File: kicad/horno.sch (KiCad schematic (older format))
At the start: 3 parts, among them P4 CONN_01X02, Q1 BC547

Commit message: modificaciones del proyecto Kicad
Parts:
- added P7: CONN_02X11, Pin_Headers:Pin_Header_Straight_2x11, symbol CONN_02X11
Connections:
- new net LCD_D0: P7.7 (P7)
- new net LCD_D1: P7.8 (P8)
- new net LCD_D2: P7.9 (P9)
- new net LCD_D3: P7.10 (P10)
- new net LCD_D4: P7.11 (P11)
- new net LCD_D5: P7.12 (P12)
- new net LCD_D6: P7.13 (P13)
- new net LCD_D7: P7.14 (P14)
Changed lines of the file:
@@
 encoding utf-8
 Sheet 1 5
-Title "Circuitos digital y analógicos"
+Title "Esquemático jerárquico"
 Date "2016-08-27"
 Rev "1"
@@
 S 2100 3700 1400 850
 U 57C2159A
-F0 "Amplificador LM35" 60
+F0 "LM35" 60
 F1 "AmpLM35.sch" 60
 F2 "+5V" I L 2100 3800 60
@@
 F5 "LM35_OUT" O R 3500 3950 60
 $EndSheet
-Wire Wire Line
-	3500 3950 4300 3950
 $Sheet
 S 2100 2700 1400 750
 U 57C52EB8
-F0 "Amplificador Termocupla" 60
+F0 "Termocupla" 60
 F1 "AmpTermocupla.sch" 60
 F2 "TERMOCUPLA_OUT" O R 3500 2800 60
@@
 F5 "GND" I L 2100 3350 60
 $EndSheet
-Wire Wire Line
-	3500 2800 3850 2800
-Wire Wire Line
-	3850 2800 3850 3850
-Wire Wire Line
-	3850 3850 4300 3850
 $Sheet
 S 6300 4550 1100 1450
 U 57C5E497
-F0 "Driver del motor paso a paso" 60
+F0 "Motor paso a paso" 60
 F1 "motorPP.sch" 60
 F2 "S1" I L 6300 5050 60
@@
 	0    1    1    0
 $EndComp
-Wire Wire Line
-	5450 3300 5850 3300
 $Comp
 L BC547 Q1
@@
 F 0 "Q1" H 6800 3375 50  0000 L CNN
 F 1 "BC547" H 6800 3300 50  0000 L CNN
-F 2 "TO_SOT_Packages_THT:TO-92_Inline_Narrow_Oval" H 6800 3225 50  0000 L CIN
+F 2 "TO_SOT_Packages_THT:TO-92_Inline_Narrow_Oval" H 6800 3225 50  0001 L CIN
 F 3 "" H 6600 3300 50  0000 L CNN
 	1    6600 3300
 	1    0    0    -1
 $EndComp
-Wire Wire Line
-	6150 3300 6400 3300
 $Comp
 L GND #PWR01
@@
 	1    0    0    -1
 $EndComp
-Wire Wire Line
-	6700 3500 6700 3650
 $Comp
 L CONN_01X02 P4
@@
 	1    0    0    -1
 $EndComp
+$Comp
+L CONN_02X11 P7
+U 1 1 57C3EF67
+P 2350 6650
+F 0 "P7" H 2350 7250 50  0000 C CNN
+F 1 "CONN_02X11" V 2350 6650 50  0000 C CNN
+F 2 "Pin_Headers:Pin_Header_Straight_2x11" H 2350 5450 50  0001 C CNN
+F 3 "" H 2350 5450 50  0000 C CNN
+	1    2350 6650
+	1    0    0    -1
+$EndComp
+Wire Wire Line
+	3500 3950 4300 3950
+Wire Wire Line
+	3500 2800 3850 2800
+Wire Wire Line
+	3850 2800 3850 3850
+Wire Wire Line
+	3850 3850 4300 3850
+Wire Wire Line
+	5450 3300 5850 3300
+Wire Wire Line
+	6150 3300 6400 3300
+Wire Wire Line
+	6700 3500 6700 3650
 Wire Wire Line
 	6700 2300 6700 2600
@@
 Wire Wire Line
 	5450 5350 6300 5350
+Wire Wire Line
+	4300 4700 3650 4700
+Wire Wire Line
+	4300 4800 3650 4800
+Wire Wire Line
+	4300 4900 3650 4900
+Wire Wire Line
+	4300 5000 3650 5000
+Wire Wire Line
+	4300 5100 3650 5100
+Text Label 3650 4700 0    60   ~ 0
+LCD_D0
+Text Label 3650 4800 0    60   ~ 0
+LCD_D1
+Text Label 3650 4900 0    60   ~ 0
+LCD_D2
+Text Label 3650 5000 0    60   ~ 0
+LCD_D3
+Text Label 3650 5100 0    60   ~ 0
+LCD_D4
+Wire Wire Line
+	4300 5200 3650 5200
+Wire Wire Line
+	4300 5300 3650 5300
+Wire Wire Line
+	4300 5400 3650 5400
+Text Label 3650 5200 0    60   ~ 0
+LCD_D5
+Text Label 3650 5300 0    60   ~ 0
+LCD_D6
+Text Label 3650 5400 0    60   ~ 0
+LCD_D7
+Wire Wire Line
+	2100 6450 1650 6450
+Text Label 1650 6450 0    60   ~ 0
+LCD_D0
+Wire Wire Line
+	2100 6550 1650 6550
+Wire Wire Line
+	2100 6650 1650 6650
+Wire Wire Line
+	2100 6750 1650 6750
+Wire Wire Line
+	2600 6450 3050 6450
+Text Label 3050 6450 2    60   ~ 0
+LCD_D1
+Wire Wire Line
+	2600 6550 3050 6550
+Wire Wire Line
+	2600 6650 3050 6650
+Wire Wire Line
+	2600 6750 3050 6750
+Text Label 3050 6550 2    60   ~ 0
+LCD_D3
+Text Label 3050 6650 2    60   ~ 0
+LCD_D5
+Text Label 3050 6750 2    60   ~ 0
+LCD_D7
+Text Label 1650 6550 0    60   ~ 0
+LCD_D2
+Text Label 1650 6650 0    60   ~ 0
+LCD_D4
+Text Label 1650 6750 0    60   ~ 0
+LCD_D6
 $EndSCHEMATC

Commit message: circuito y pcb terminado.
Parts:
- added P10: Alimentación, Pin_Headers:Pin_Header_Straight_1x03, symbol CONN_01X03
- P4: value CONN_01X02 -> TRIAC
- P7: value CONN_02X11 -> Pantalla
- Q1: footprint TO_SOT_Packages_THT:TO-92_Inline_Narrow_Oval -> TO_SOT_Packages_THT:TO-92_Inline_Wide
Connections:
- net +5V: now also P7.2 (P2), P10.2 (P2)
- net GND: now also P7.1 (P1), P10.1 (P1)
- net LCD_CS: now reaches P7.15 (P15)
- net LCD_RST: now reaches P7.16 (P16)
- net LCD_RD: now reaches P7.4 (P4)
- net LCD_WR: now reaches P7.5 (P5)
- net LCD_A0: now reaches P7.6 (P6)
- new net -5V: P10.3 (P3)
- no-connect marks 0 -> 7
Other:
- note added: "Conector de la\nllave semiconductora"
- note added: "Conector de la\npantalla LCD"
- note added: "Entrada de \nalimentación"
- moved on the sheet: P4, Q1, R9

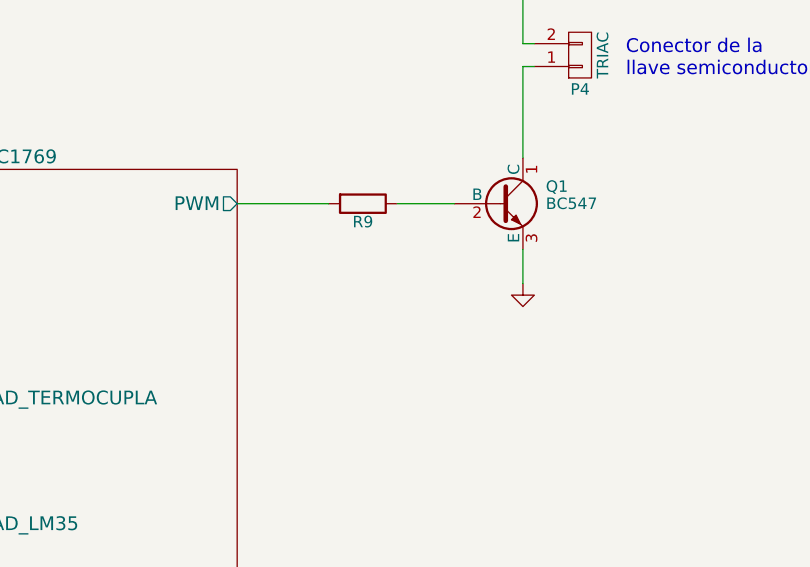
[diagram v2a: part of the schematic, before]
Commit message: R de pulldown para que la resistencia no se energice con un reset.
Cuando el microcontrolador está pasando por un reset, la pata del PWM está flotando y alcanza para activar el transistor.
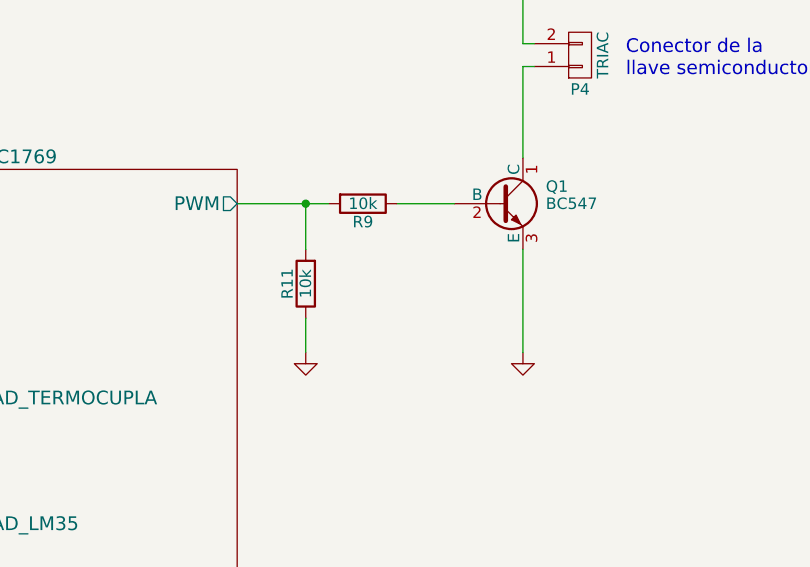
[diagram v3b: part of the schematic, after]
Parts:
- added R11: 10k, Resistors_ThroughHole:Resistor_Horizontal_RM10mm, symbol R
- R9: value R -> 10k
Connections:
- net GND: now also R11.1
- net LPC1769/PWM: now also R11.2
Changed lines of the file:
@@
 P 6000 2550
 F 0 "R9" V 6080 2550 50  0000 C CNN
-F 1 "R" V 6000 2550 50  0001 C CNN
+F 1 "10k" V 6000 2550 50  0000 C CNN
 F 2 "Resistors_ThroughHole:Resistor_Horizontal_RM10mm" V 5930 2550 50  0001 C CNN
 F 3 "" H 6000 2550 50  0000 C CNN
@@
 $EndComp
 $Comp
-L GND #PWR01
+L GND #PWR5
 U 1 1 57C67CA4
-P 6700 2900
-F 0 "#PWR01" H 6700 2650 50  0001 C CNN
-F 1 "GND" H 6700 2750 50  0001 C CNN
-F 2 "" H 6700 2900 50  0000 C CNN
-F 3 "" H 6700 2900 50  0000 C CNN
-	1    6700 2900
+P 6700 3200
+F 0 "#PWR5" H 6700 2950 50  0001 C CNN
+F 1 "GND" H 6700 3050 50  0001 C CNN
+F 2 "" H 6700 3200 50  0000 C CNN
+F 3 "" H 6700 3200 50  0000 C CNN
+	1    6700 3200
 	1    0    0    -1
 $EndComp
@@
 $EndComp
 $Comp
-L +5V #PWR02
+L +5V #PWR4
 U 1 1 57C682C4
 P 6700 1550
-F 0 "#PWR02" H 6700 1400 50  0001 C CNN
+F 0 "#PWR4" H 6700 1400 50  0001 C CNN
 F 1 "+5V" H 6700 1690 50  0000 C CNN
 F 2 "" H 6700 1550 50  0000 C CNN
@@
 	6150 2550 6400 2550
 Wire Wire Line
-	6700 2750 6700 2900
+	6700 2750 6700 3200
 Wire Wire Line
 	6700 1550 6700 1850
@@
 LCD_D6
 $Comp
-L GND #PWR03
+L GND #PWR1
 U 1 1 57C97FEB
 P 1400 6150
-F 0 "#PWR03" H 1400 5900 50  0001 C CNN
+F 0 "#PWR1" H 1400 5900 50  0001 C CNN
 F 1 "GND" H 1400 6000 50  0000 C CNN
 F 2 "" H 1400 6150 50  0000 C CNN
@@
 	2600 6150 3200 6150
 $Comp
-L +5V #PWR04
+L +5V #PWR2
 U 1 1 57C987B0
 P 3200 5950
-F 0 "#PWR04" H 3200 5800 50  0001 C CNN
+F 0 "#PWR2" H 3200 5800 50  0001 C CNN
 F 1 "+5V" H 3200 6090 50  0000 C CNN
 F 2 "" H 3200 5950 50  0000 C CNN
@@
 $EndComp
 $Comp
-L GND #PWR05
+L GND #PWR8
 U 1 1 57CBC9F7
 P 9850 2850
-F 0 "#PWR05" H 9850 2600 50  0001 C CNN
+F 0 "#PWR8" H 9850 2600 50  0001 C CNN
 F 1 "GND" H 9850 2700 50  0000 C CNN
 F 2 "" H 9850 2850 50  0000 C CNN
@@
 	9850 2650 9850 2850
 $Comp
-L +5V #PWR06
+L +5V #PWR6
 U 1 1 57CBD60F
 P 9650 2300
-F 0 "#PWR06" H 9650 2150 50  0001 C CNN
+F 0 "#PWR6" H 9650 2150 50  0001 C CNN
 F 1 "+5V" H 9650 2440 50  0000 C CNN
 F 2 "" H 9650 2300 50  0000 C CNN
@@
 $EndComp
 $Comp
-L -5V #PWR6
+L -5V #PWR7
 U 1 1 57CBD782
 P 9850 2300
-F 0 "#PWR6" H 9850 2400 50  0001 C CNN
+F 0 "#PWR7" H 9850 2400 50  0001 C CNN
 F 1 "-5V" H 9850 2450 50  0000 C CNN
 F 2 "" H 9850 2300 50  0000 C CNN
@@
 Wire Wire Line
 	9650 2550 9650 2300
+$Comp
+L R R11
+U 1 1 581CDAE7
+P 5750 2900
+F 0 "R11" V 5830 2900 50  0000 C CNN
+F 1 "10k" V 5750 2900 50  0000 C CNN
+F 2 "Resistors_ThroughHole:Resistor_Horizontal_RM10mm" V 5680 2900 50  0001 C CNN
+F 3 "" H 5750 2900 50  0000 C CNN
+	1    5750 2900
+	-1   0    0    1
+$EndComp
+Wire Wire Line
+	5750 2750 5750 2550
+Connection ~ 5750 2550
+Wire Wire Line
+	5750 3200 5750 3050
+$Comp
+L GND #PWR?
+U 1 1 581CDFB6
+P 5750 3200
+F 0 "#PWR?" H 5750 2950 50  0001 C CNN
+F 1 "GND" H 5750 3050 50  0001 C CNN
+F 2 "" H 5750 3200 50  0000 C CNN
+F 3 "" H 5750 3200 50  0000 C CNN
+	1    5750 3200
+	1    0    0    -1
+$EndComp
 $EndSCHEMATC

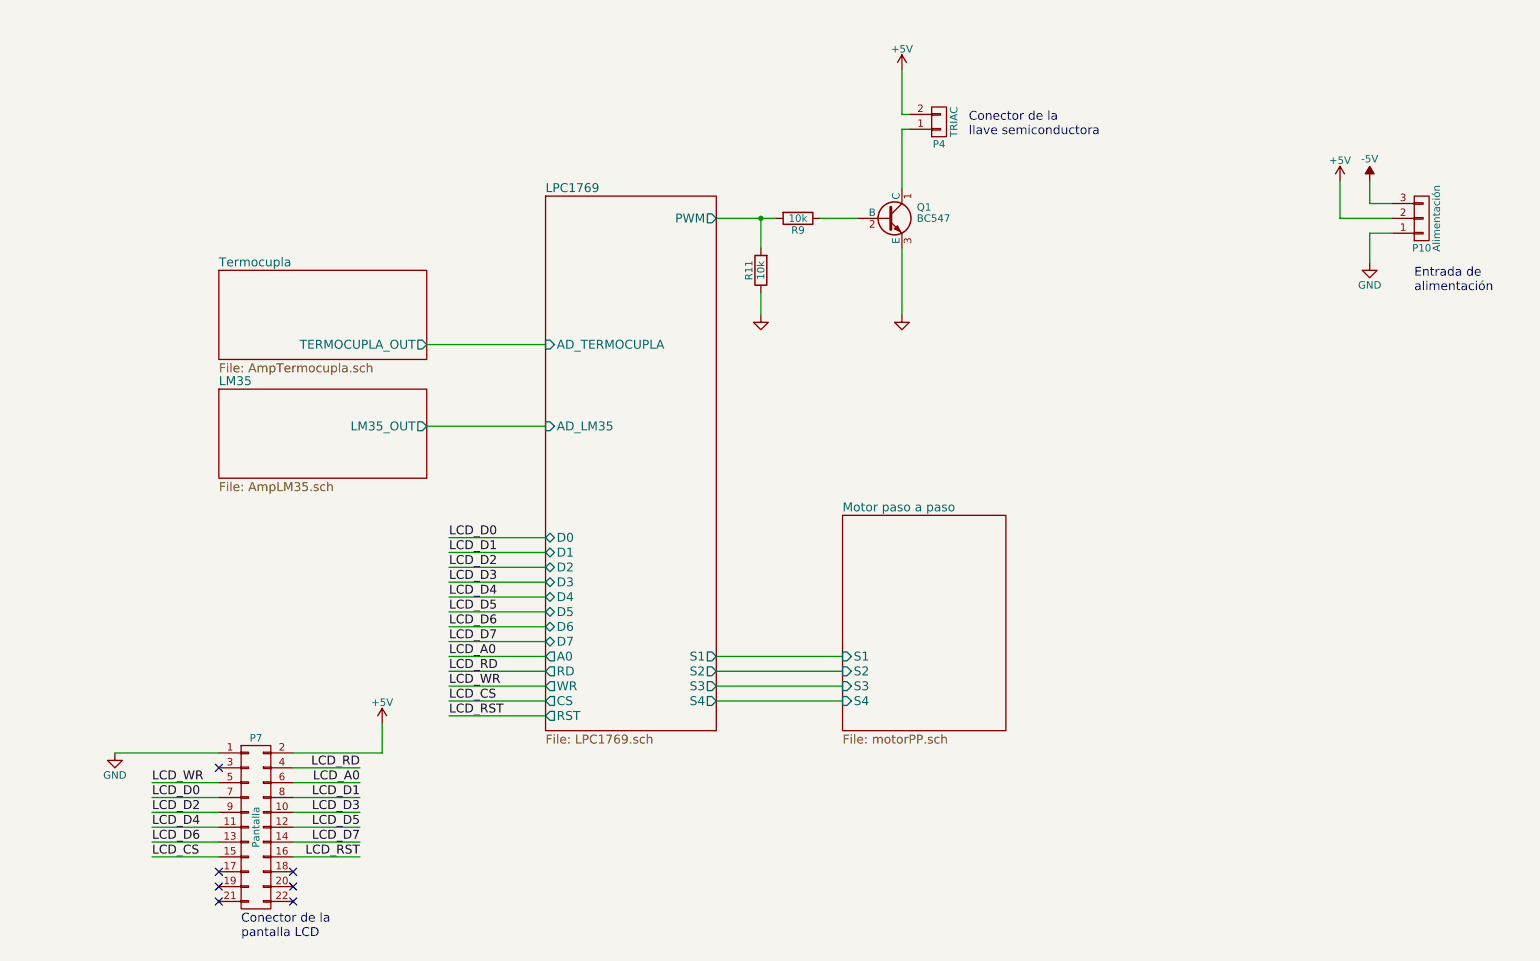
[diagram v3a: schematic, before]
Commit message: Actualizar los esquemáticos
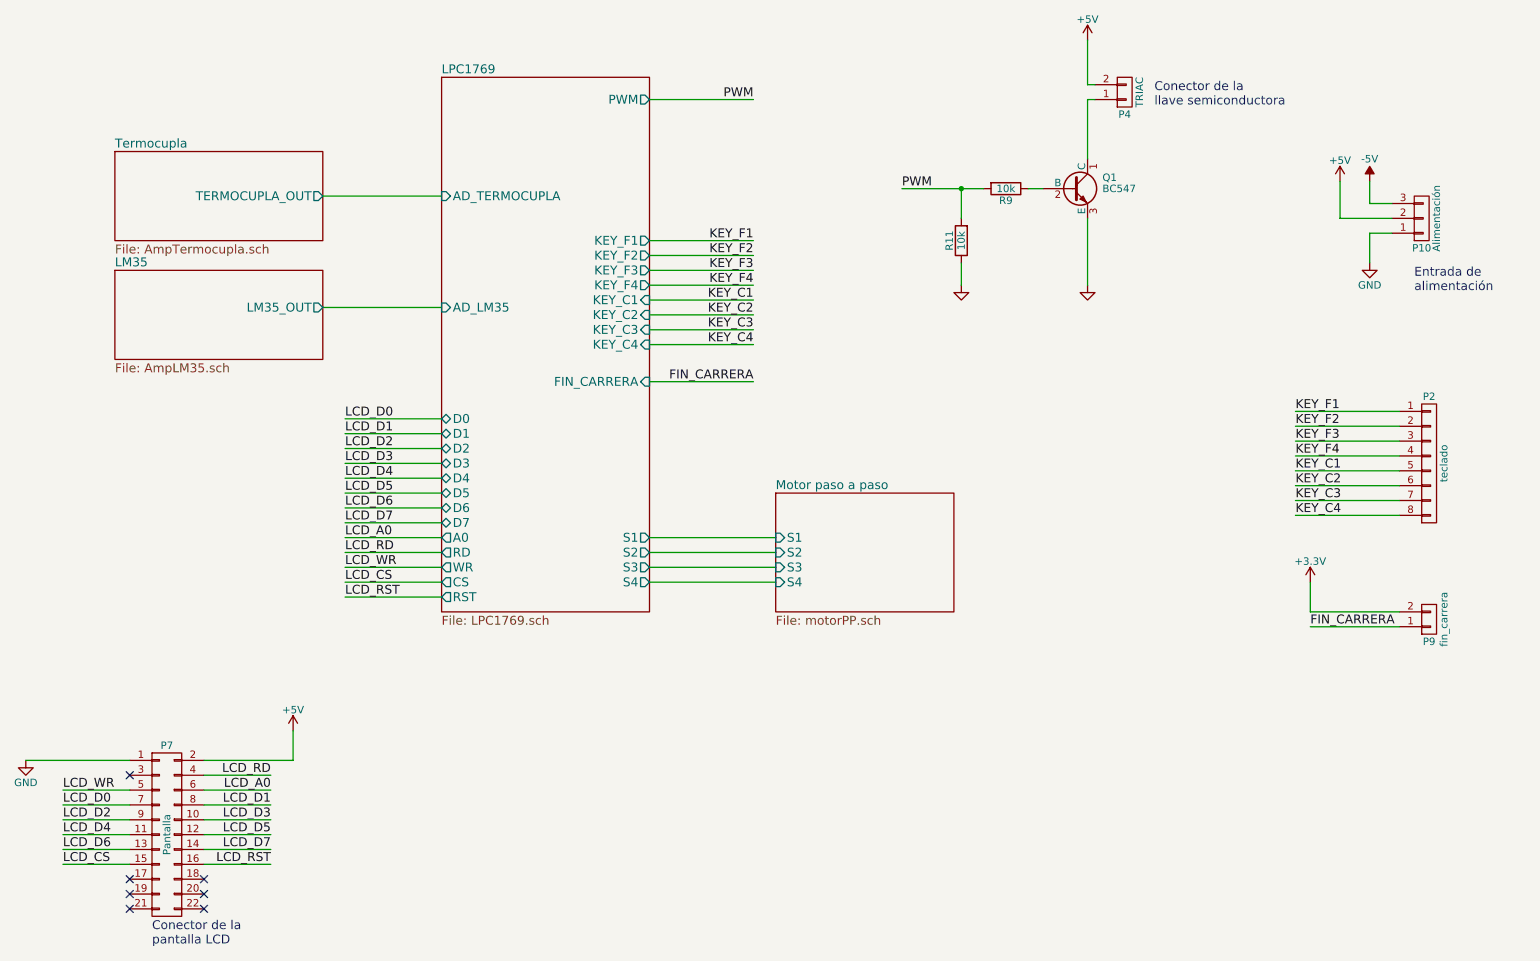
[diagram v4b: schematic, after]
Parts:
- added P2: teclado, symbol CONN_01X08
- added P9: fin_carrera, symbol CONN_01X02
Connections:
- net LPC1769/PWM renamed PWM
- new net +3V3: P9.2 (P2)
- new net FIN_CARRERA: P9.1 (P1)
- new net KEY_C1: P2.5 (P5)
- new net KEY_C2: P2.6 (P6)
- new net KEY_C3: P2.7 (P7)
- new net KEY_C4: P2.8 (P8)
- new net KEY_F1: P2.1 (P1)
- new net KEY_F2: P2.2 (P2)
- new net KEY_F3: P2.3 (P3)
- new net KEY_F4: P2.4 (P4)
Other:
- moved on the sheet: P4, P7, Q1, R11, R9

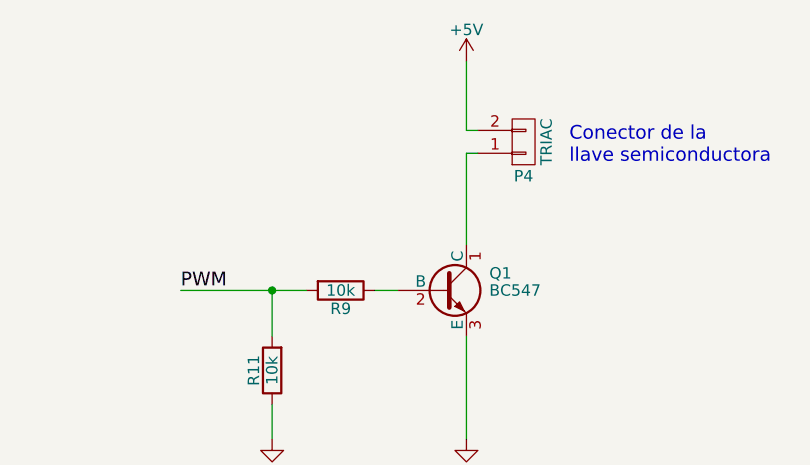
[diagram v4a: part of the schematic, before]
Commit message: actualizar el esquematico rev3
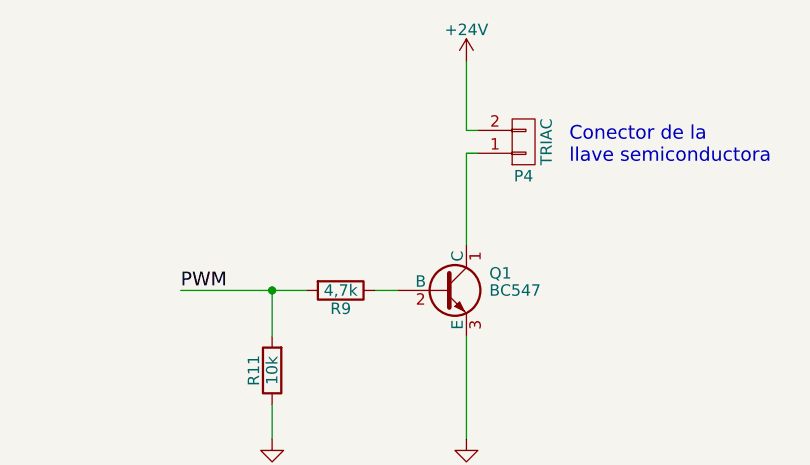
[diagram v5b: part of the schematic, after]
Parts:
- R9: value 10k -> 4,7k
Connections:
- net +5V: no longer P4.2 (P2)
- new net +24V: P4.2 (P2)
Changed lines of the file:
@@
 P 7400 2350
 F 0 "R9" V 7480 2350 50  0000 C CNN
-F 1 "10k" V 7400 2350 50  0000 C CNN
+F 1 "4,7k" V 7400 2350 50  0000 C CNN
 F 2 "Resistors_ThroughHole:Resistor_Horizontal_RM10mm" V 7330 2350 50  0001 C CNN
 F 3 "" H 7400 2350 50  0000 C CNN
@@
 	1    8200 1700
 	1    0    0    1
-$EndComp
-$Comp
-L +5V #PWR4
-U 1 1 57C682C4
-P 7950 1350
-F 0 "#PWR4" H 7950 1200 50  0001 C CNN
-F 1 "+5V" H 7950 1490 50  0000 C CNN
-F 2 "" H 7950 1350 50  0000 C CNN
-F 3 "" H 7950 1350 50  0000 C CNN
-	1    7950 1350
-	1    0    0    -1
 $EndComp
 $Comp
@@
 Wire Wire Line
 	9450 5000 9450 5200
+$Comp
+L +24V #PWR4
+U 1 1 582F3DCD
+P 7950 1350
+F 0 "#PWR4" H 7950 1200 50  0001 C CNN
+F 1 "+24V" H 7950 1490 50  0000 C CNN
+F 2 "" H 7950 1350 50  0000 C CNN
+F 3 "" H 7950 1350 50  0000 C CNN
+	1    7950 1350
+	1    0    0    -1
+$EndComp
 $EndSCHEMATC

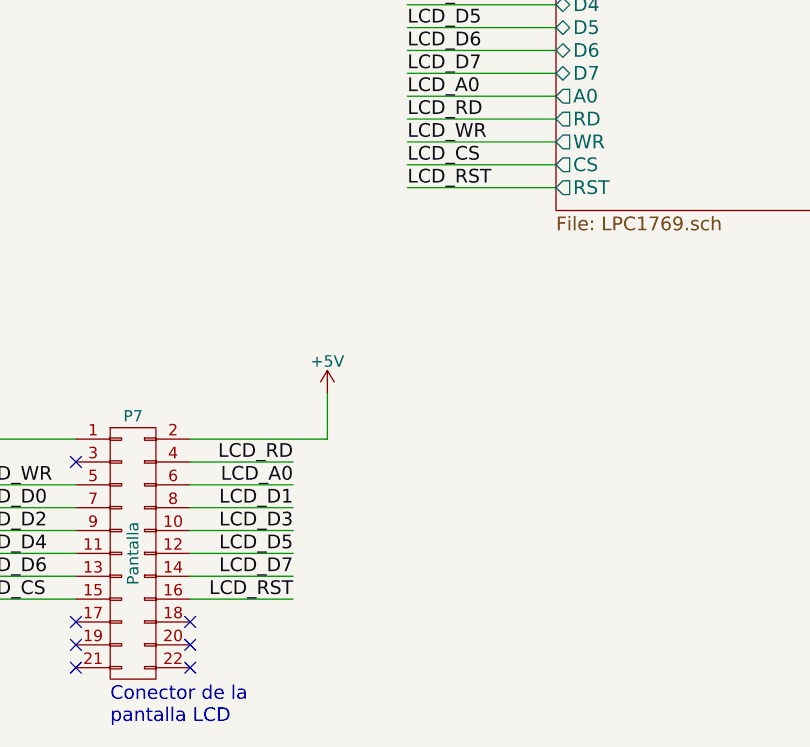
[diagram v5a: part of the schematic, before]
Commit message: Poner la pata de RST del display a 5V
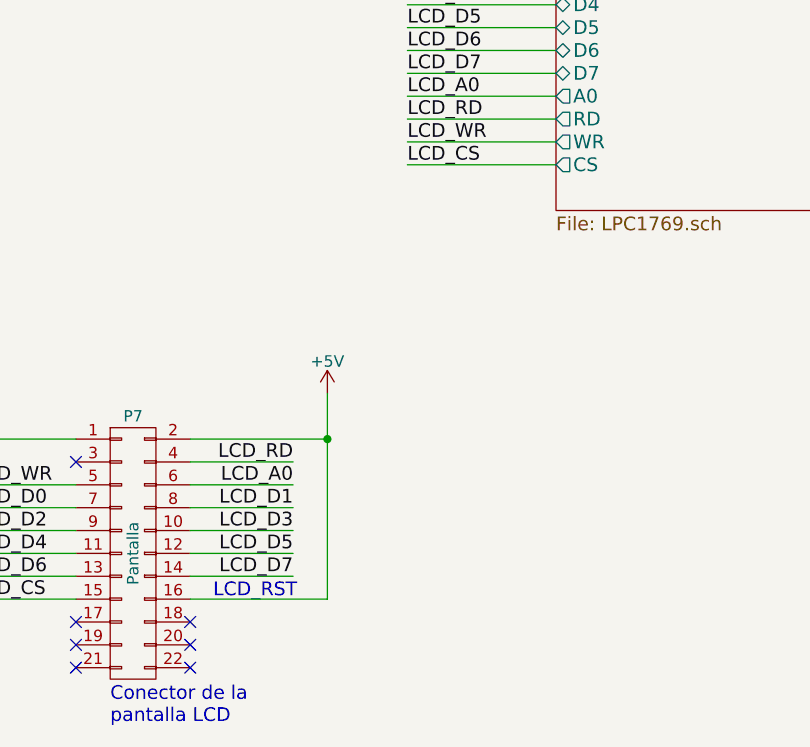
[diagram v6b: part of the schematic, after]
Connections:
- net LCD_RST is gone; now on net +5V: P7.16 (P16)
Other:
- note added: "LCD_RST"
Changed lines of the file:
@@
 Text Notes 10150 3050 0    60   ~ 0
 Entrada de \nalimentación
-Text Label 2950 5100 0    60   ~ 0
-LCD_RST
-Text Label 2450 6900 2    60   ~ 0
-LCD_RST
 NoConn ~ 2000 7000
 $Comp
@@
 F19 "AD_TERMOCUPLA" I L 3600 2400 60
 F20 "AD_LM35" I L 3600 3150 60
-F21 "RST" O L 3600 5100 60
-F22 "KEY_F1" O R 5000 2700 60
-F23 "KEY_F2" O R 5000 2800 60
-F24 "KEY_F3" O R 5000 2900 60
-F25 "KEY_F4" O R 5000 3000 60
-F26 "KEY_C1" I R 5000 3100 60
-F27 "KEY_C2" I R 5000 3200 60
-F28 "KEY_C3" I R 5000 3300 60
-F29 "KEY_C4" I R 5000 3400 60
-F30 "FIN_CARRERA" I R 5000 3650 60
+F21 "KEY_F1" O R 5000 2700 60
+F22 "KEY_F2" O R 5000 2800 60
+F23 "KEY_F3" O R 5000 2900 60
+F24 "KEY_F4" O R 5000 3000 60
+F25 "KEY_C1" I R 5000 3100 60
+F26 "KEY_C2" I R 5000 3200 60
+F27 "KEY_C3" I R 5000 3300 60
+F28 "KEY_C4" I R 5000 3400 60
+F29 "FIN_CARRERA" I R 5000 3650 60
 $EndSheet
 Wire Wire Line
@@
 	2800 2400 3600 2400
 Wire Wire Line
-	3600 5100 2950 5100
-Wire Wire Line
-	2600 6200 2600 6000
-Wire Wire Line
-	2000 6900 2450 6900
+	2600 6900 2600 6000
+Wire Wire Line
+	2000 6900 2600 6900
 Wire Wire Line
 	10000 2450 9850 2450
@@
 	1    0    0    -1
 $EndComp
+Connection ~ 2600 6200
+Text Notes 2100 6900 0    60   ~ 0
+LCD_RST
 $EndSCHEMATC
